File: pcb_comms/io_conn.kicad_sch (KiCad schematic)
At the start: 17 parts, among them IC3 CP2102N-A02-GQFN28, J1 Conn_01x06_Pin, J2 Conn_02x20_Counter_Clockwise, J3 Conn_02x08_Counter_Clockwise, J7 USB-B-Micro

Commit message: Update pinout
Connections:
- net AUX10: now also J3.12 (Pin_12); no longer J3.10 (Pin_10)
- net AUX6: now also J3.14 (Pin_14); no longer J3.12 (Pin_12)
- net AUX7: now also J3.15 (Pin_15); no longer J3.13 (Pin_13)
- net AUX8: now also J3.16 (Pin_16); no longer J3.14 (Pin_14)
- net AUX9: now also J3.13 (Pin_13); no longer J3.11 (Pin_11)
- no-connect marks 41 -> 43

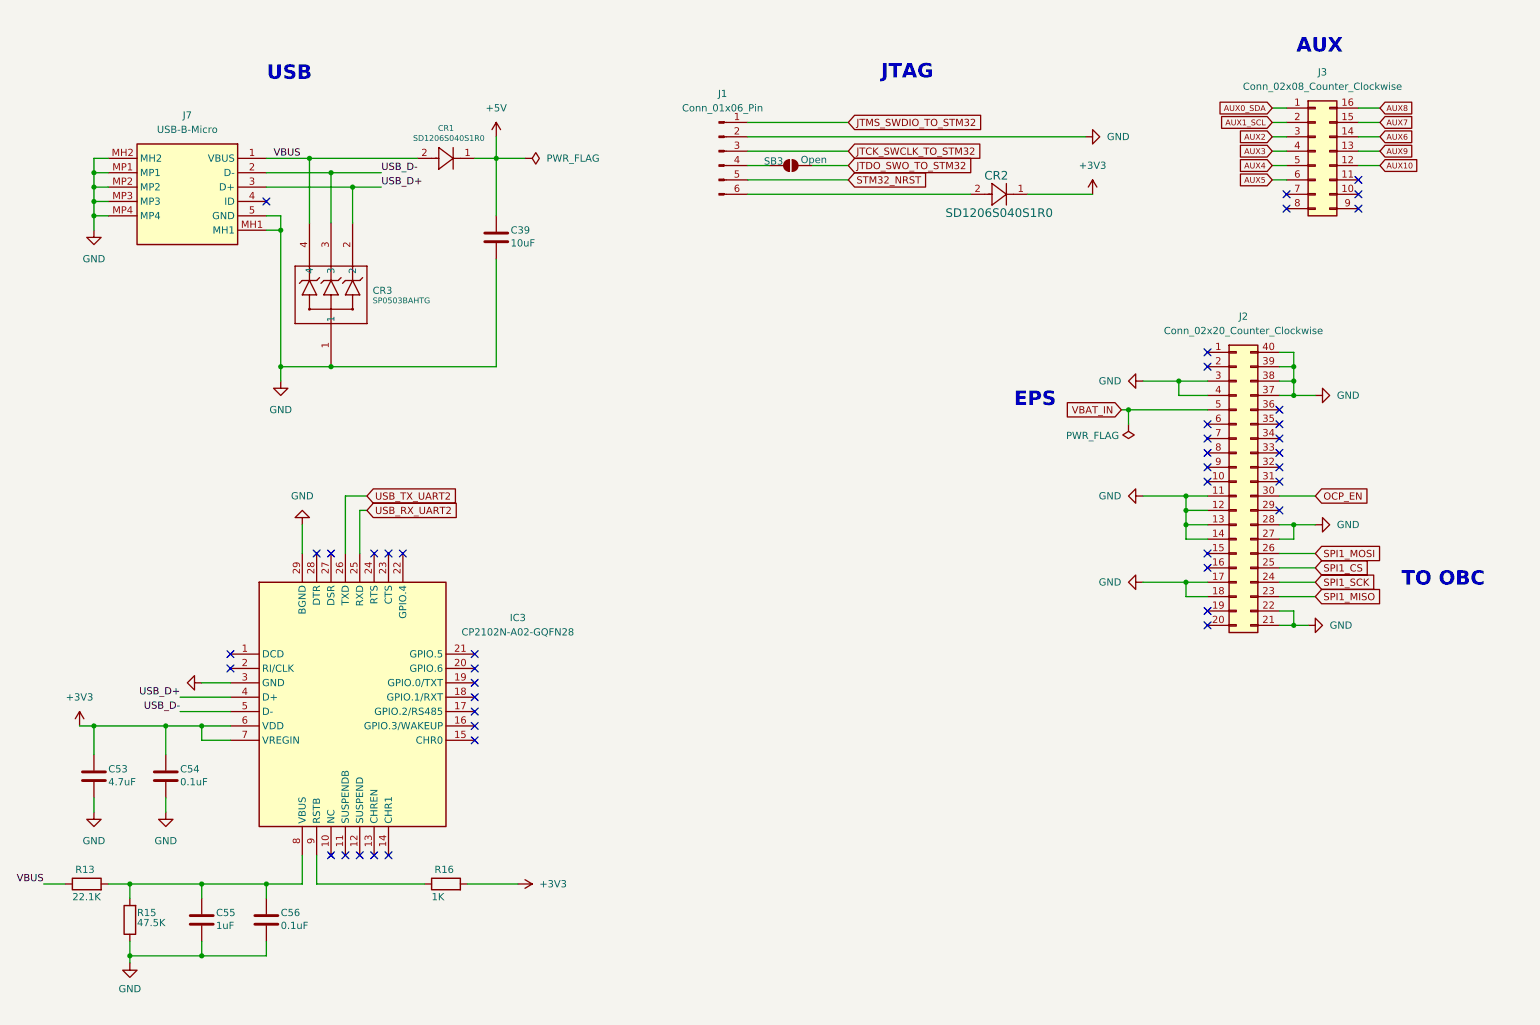
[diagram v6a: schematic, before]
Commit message: Update schematic. Add net classes and JST footprints for aux
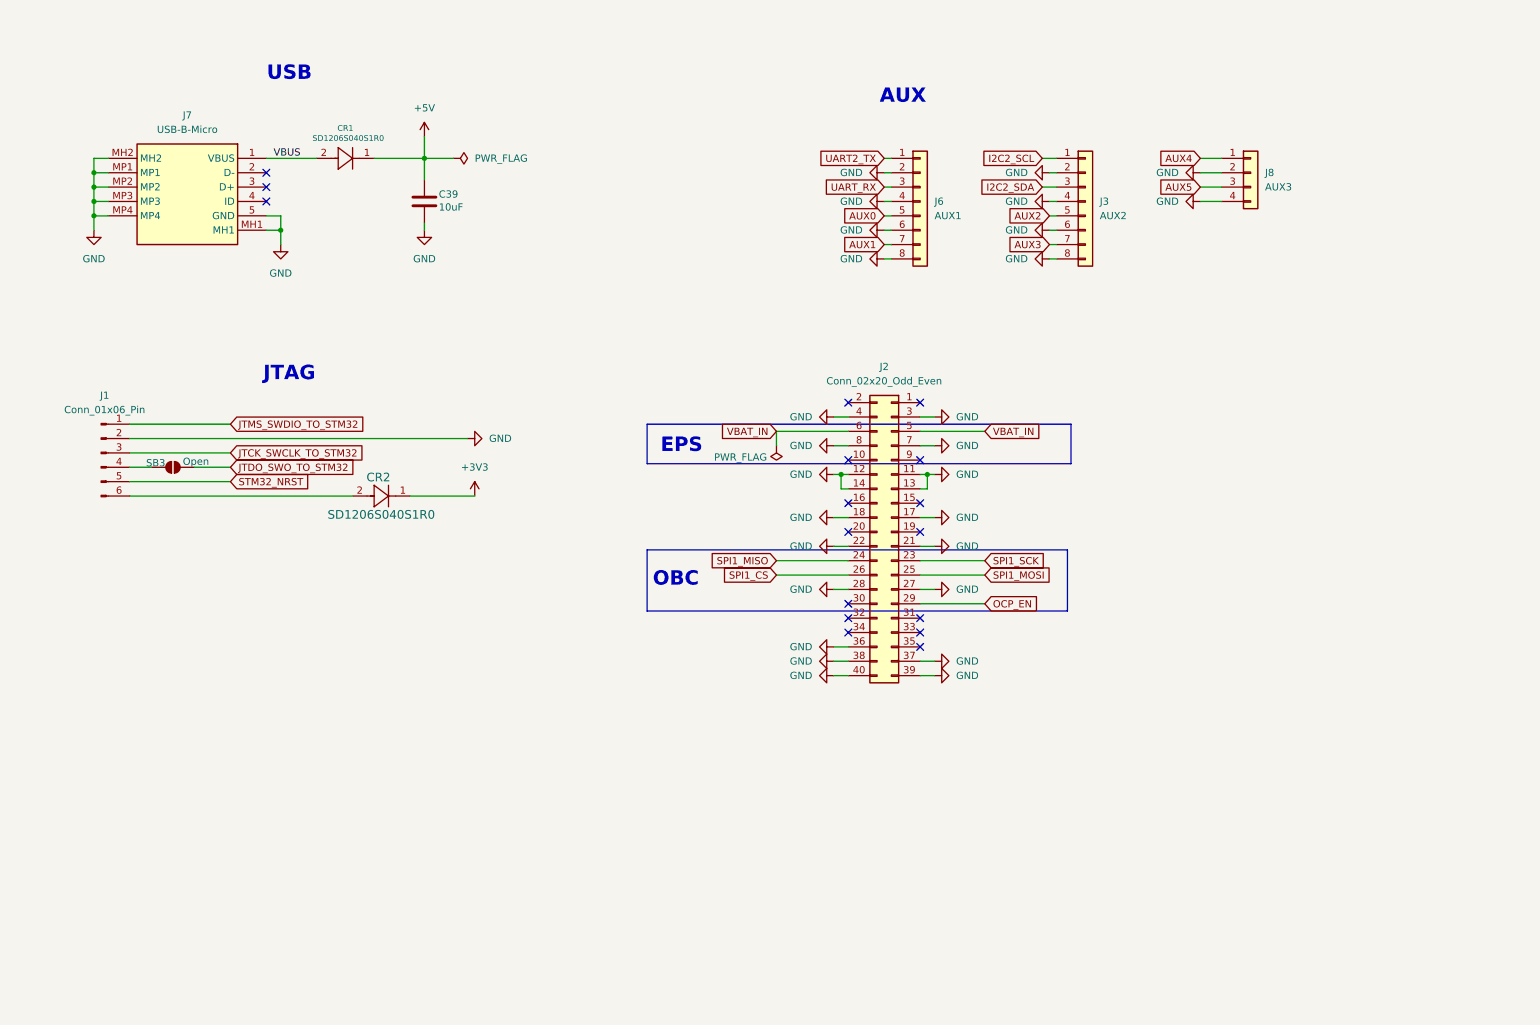
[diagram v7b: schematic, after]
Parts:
- removed C53: 4.7uF, Capacitor_SMD:C_0805_2012Metric_Pad1.18x1.45mm_HandSolder, symbol Device:C
- removed C54, C56: 0.1uF, Capacitor_SMD:C_0805_2012Metric_Pad1.18x1.45mm_HandSolder, symbol Device:C
- removed C55: 1uF, Capacitor_SMD:C_0805_2012Metric_Pad1.18x1.45mm_HandSolder, symbol Device:C
- removed CR3: SP0503BAHTG, ESD_PROTECTION_DIODE_SP0503BAHTG:ESD_PROTECTION_DIODE_SP0503BAHTG, symbol ESD_PROTECTION_DIODE_SP0503BAHTG:SP0503BAHTG
- removed IC3: CP2102N-A02-GQFN28, USB_TO_UART_BRIDGE_CP2102N:USB_TO_UART_BRIDGE_CP2102N-A02-GQFN28, symbol USB_TO_UART_BRIDGE_CP2102N-A02-GQFN28:CP2102N-A02-GQFN28
- removed J2: Conn_02x20_Counter_Clockwise, Connector_PinSocket_2.54mm:PinSocket_2x20_P2.54mm_Vertical, symbol Connector_Generic:Conn_02x20_Counter_Clockwise
- removed J3: Conn_02x08_Counter_Clockwise, Connector_PinSocket_2.54mm:PinSocket_2x08_P2.54mm_Vertical_SMD, symbol Connector_Generic:Conn_02x08_Counter_Clockwise
- removed R13: 22.1K, Resistor_SMD:R_0805_2012Metric_Pad1.20x1.40mm_HandSolder, symbol Device:R
- removed R15: 47.5K, Resistor_SMD:R_0805_2012Metric_Pad1.20x1.40mm_HandSolder, symbol Device:R
- removed R16: 1K, Resistor_SMD:R_0805_2012Metric_Pad1.20x1.40mm_HandSolder, symbol Device:R
- added J2: Conn_02x20_Odd_Even, Connector_PinSocket_2.54mm:PinSocket_2x20_P2.54mm_Vertical, symbol Connector_Generic:Conn_02x20_Odd_Even
- added J3: AUX2, Connector_PinSocket_2.54mm:PinSocket_1x08_P2.54mm_Vertical, symbol Connector_Generic:Conn_01x08
- added J6: AUX1, Connector_PinSocket_2.54mm:PinSocket_1x08_P2.54mm_Vertical, symbol Connector_Generic:Conn_01x08
- added J8: AUX3, Connector_PinSocket_2.54mm:PinSocket_1x04_P2.54mm_Vertical, symbol Connector_Generic:Conn_01x04
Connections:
- net AUX2: now also J3.5 (Pin_5)
- net AUX3: now also J3.7 (Pin_7)
- net AUX4: now also J8.1 (Pin_1)
- net AUX5: now also J8.3 (Pin_3)
- net GND: now also J2.11 (Pin_11), J2.12 (Pin_12), J2.13 (Pin_13), J2.14 (Pin_14), J2.17 (Pin_17), J2.18 (Pin_18), J2.21 (Pin_21), J2.22 (Pin_22), J2.27 (Pin_27), J2.28 (Pin_28), J2.3 (Pin_3), J2.36 (Pin_36), J2.37 (Pin_37), J2.38 (Pin_38), J2.39 (Pin_39), J2.4 (Pin_4), J2.40 (Pin_40), J2.7 (Pin_7), J2.8 (Pin_8), J3.2 (Pin_2), J3.4 (Pin_4), J3.6 (Pin_6), J3.8 (Pin_8), J6.2 (Pin_2), J6.4 (Pin_4), J6.6 (Pin_6), J6.8 (Pin_8), J8.2 (Pin_2), J8.4 (Pin_4)
- net OCP_EN: now also J2.29 (Pin_29)
- net SPI1_CS: now also J2.26 (Pin_26)
- net SPI1_MISO: now also J2.24 (Pin_24)
- net SPI1_MOSI: now also J2.25 (Pin_25)
- net SPI1_SCK: now also J2.23 (Pin_23)
- net VBAT_IN: now also J2.5 (Pin_5), J2.6 (Pin_6)
- net USB_D+: no longer names the net of J7.3 (D+)
- net USB_D-: no longer names the net of J7.2 (D-)
- new net AUX0: J6.5 (Pin_5)
- new net AUX1: J6.7 (Pin_7)
- new net I2C2_SCL: J3.1 (Pin_1)
- new net I2C2_SDA: J3.3 (Pin_3)
- new net UART2_TX: J6.1 (Pin_1)
- new net UART_RX: J6.3 (Pin_3)
- no-connect marks 43 -> 17
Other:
- note added: "OBC"
- note removed: "TO OBC"
- moved on the sheet: C39, CR1, CR2, J1, SB3

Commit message: Update pcb
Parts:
- removed J8: AUX3, Connector_PinSocket_2.54mm:PinSocket_1x04_P2.54mm_Vertical, symbol Connector_Generic:Conn_01x04
- added J8: AUX2, Connector_PinSocket_2.54mm:PinSocket_1x08_P2.54mm_Vertical, symbol Connector_Generic:Conn_01x08
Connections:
- net AUX4: now also J8.1 (Pin_1)
- net AUX5: now also J8.3 (Pin_3)
- net GND: now also J8.2 (Pin_2), J8.4 (Pin_4)
- no-connect marks 17 -> 21
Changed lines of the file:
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@@
+	)
+	(no_connect
+		(at 228.6 60.96)
 	)
 	(no_connect
@@
 	)
 	(no_connect
+		(at 228.6 55.88)
+	)
+	(no_connect
 		(at 175.26 124.46)
 	)
@@
 	)
 	(no_connect
+		(at 228.6 58.42)
+	)
+	(no_connect
 		(at 175.26 129.54)
 	)
@@
 	(no_connect
 		(at 175.26 109.22)
+	)
+	(no_connect
+		(at 228.6 53.34)
 	)
 	(no_connect
@@
 	)
 	(symbol
-		(lib_id "Connector_Generic:Conn_01x04")
-		(at 233.68 45.72 0)
-		(unit 1)
-		(exclude_from_sim no)
-		(in_bom yes)
-		(on_board yes)
-		(dnp no)
-		(fields_autoplaced yes)
-		(property "Reference" "J8"
-			(at 236.22 45.7199 0)
-			(effects
-				(font
-					(size 1.27 1.27)
-				)
-				(justify left)
-			)
-		)
-		(property "Value" "AUX3"
-			(at 236.22 48.2599 0)
-			(effects
-				(font
-					(size 1.27 1.27)
-				)
-				(justify left)
-			)
-		)
-		(property "Footprint" "Connector_PinSocket_2.54mm:PinSocket_1x04_P2.54mm_Vertical"
-			(at 233.68 45.72 0)
-			(effects
-				(font
-					(size 1.27 1.27)
-				)
-				(hide yes)
-			)
-		)
-		(property "Datasheet" "~"
-			(at 233.68 45.72 0)
-			(effects
-				(font
-					(size 1.27 1.27)
-				)
-				(hide yes)
-			)
-		)
-		(property "Description" "Generic connector, single row, 01x04, script generated (kicad-library-utils/schlib/autogen/connector/)"
-			(at 233.68 45.72 0)
-			(effects
-				(font
-					(size 1.27 1.27)
-				)
-				(hide yes)
-			)
-		)
-		(pin "1"
-		)
-		(pin "2"
-		)
-		(pin "3"
-		)
-		(pin "4"
-		)
-		(instances
-			(project ""
-				(path "/ea597178-b44d-4db9-826c-8f86e8d231f0/a4d41170-f1e3-4812-89ef-2aa6a238f022"
-					(reference "J8")
-					(unit 1)
-				)
-			)
-		)
-	)
-	(symbol
 		(lib_id "power:GND")
 		(at 87.63 55.88 0)
@@
 					(unit 1)
 				)
+			)
+		)
+	)
+	(symbol
+		(lib_id "Connector_Generic:Conn_01x08")
+		(at 233.68 50.8 0)
+		(unit 1)
+		(exclude_from_sim no)
+		(in_bom yes)
+		(on_board yes)
+		(dnp no)
+		(fields_autoplaced yes)
+		(property "Reference" "J8"
+			(at 236.22 50.7999 0)
+			(effects
+				(font
+					(size 1.27 1.27)
+				)
+				(justify left)
+			)
+		)
+		(property "Value" "AUX2"
+			(at 236.22 53.3399 0)
+			(effects
+				(font
+					(size 1.27 1.27)
+				)
+				(justify left)
+			)
+		)
+		(property "Footprint" "Connector_PinSocket_2.54mm:PinSocket_1x08_P2.54mm_Vertical"
+			(at 233.68 50.8 0)
+			(effects
+				(font
+					(size 1.27 1.27)
+				)
+				(hide yes)
+			)
+		)
+		(property "Datasheet" "~"
+			(at 233.68 50.8 0)
+			(effects
+				(font
+					(size 1.27 1.27)
+				)
+				(hide yes)
+			)
+		)
+		(property "Description" "Generic connector, single row, 01x08, script generated (kicad-library-utils/schlib/autogen/connector/)"
+			(at 233.68 50.8 0)
+			(effects
+				(font
+					(size 1.27 1.27)
+				)
+				(hide yes)
+			)
+		)
+		(pin "2"
+		)
+		(pin "5"
+		)
+		(pin "1"
+		)
+		(pin "8"
+		)
+		(pin "3"
+		)
+		(pin "4"
+		)
+		(pin "6"
+		)
+		(pin "7"
+		)
+		(instances
+			(project "pcb_comms_board"
+				(path "/ea597178-b44d-4db9-826c-8f86e8d231f0/a4d41170-f1e3-4812-89ef-2aa6a238f022"
+					(reference "J8")
+					(unit 1)
+				)
